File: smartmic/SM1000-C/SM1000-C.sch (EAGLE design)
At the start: 194 parts, among them CN1 HDR100-3, CN10 MJ-3523-SMT, CN11 HDR100-3, CN12 DF11-16DS, CN2 MOLEX-MINI-B-SMT, CN3 RASM722PX, CN4 RJ-45, CN5 MJ-3523-SMT, CN6 SJ-3524, CN7 MJ-3523-SMT, CN8 SJ-3524, CN9 MJ-3523-SMT, J1 JMP-2PIN, J3 JMP-2PIN, J4 JMP-2PIN, P1 TPAD50, P10 TPAD50, P11 TPAD50, P12 TPAD50, P13 TPAD50, P14 TPAD50, P15 TPAD50, P16 TPAD50, P17 TPAD50, P18 TPAD50, P19 TPAD50, P2 TPAD50, P20 TPAD50, P3 TPAD50, P4 TPAD50, P5 TPAD50, P6 TPAD50, P7 TPAD50, P8 TPAD50, P9 TPAD50, SW1 SW-BOURNS-7914S, SW2 SW-BOURNS-7914S, SW3 DPDT, SW4 SW-BOURNS-7914S, SW5 SW-BOURNS-7914J, T1 SM-LP-5001, T2 SM-LP-5001, U1 STM32F405, U2 LD3985M33R, U3 STMPS2141, U4 EMIF02-USB03F2, U5 TPS54329E, U6 LMV341, U7 LMV341, U8 LM386M-1, U9 LMV341

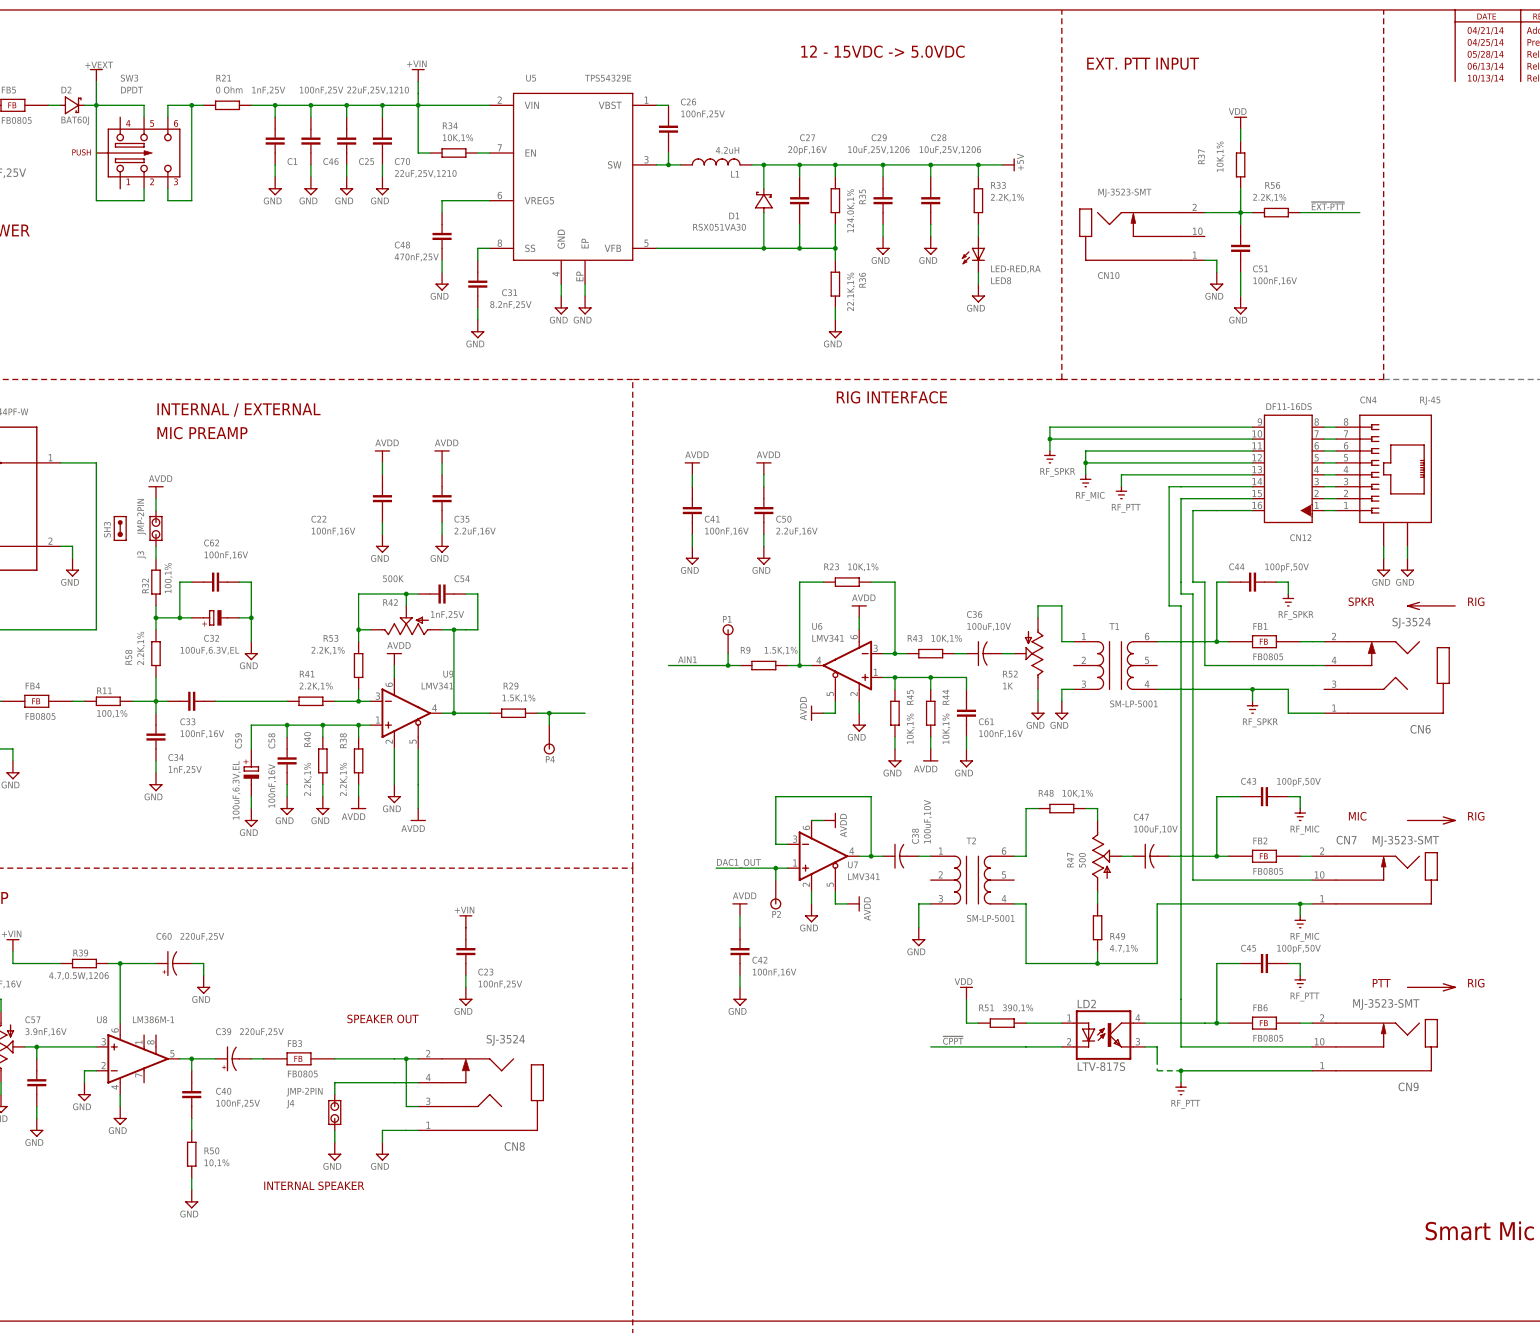
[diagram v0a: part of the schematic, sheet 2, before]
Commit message: Update SM1000-C schematics RGB
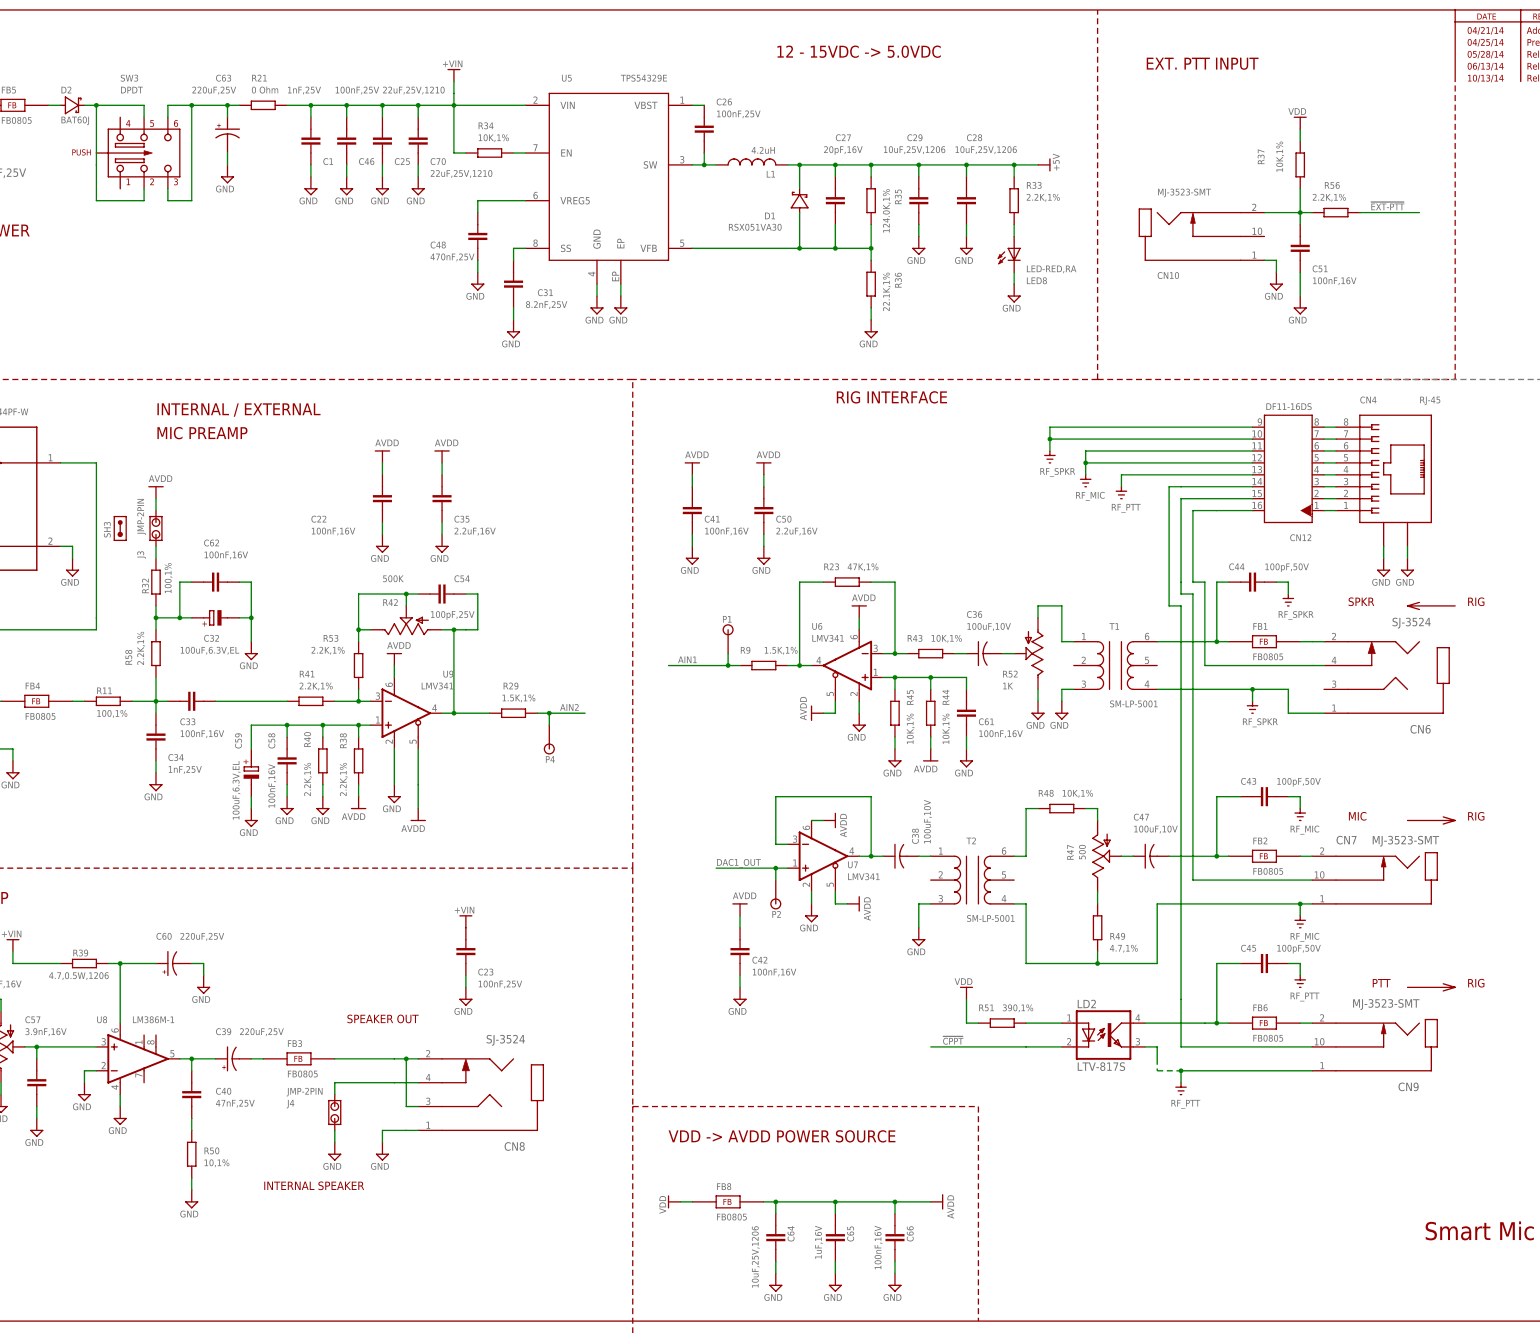
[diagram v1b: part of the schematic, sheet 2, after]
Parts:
- added C63: 220uF,25V, _RoweTel:CAP-CHEMI-MVE-HA0
- added C64: 10uF,25V,1206, ipc-7351-capacitor:CAPACITOR_1206
- added C65: 1uF,16V, AA-ipc-7351-capacitor:CAPACITOR_0603
- added C66: 100nF,16V, AA-ipc-7351-capacitor:CAPACITOR_0603
- added FB8: FB0805, _RoweTel:FB0805
- C40: value 100nF,25V -> 47nF,25V
- C54: value 1nF,25V -> 100pF,25V
- CN3: device _RoweTel:RASM712PX -> _RoweTel:RASM722PX
- R18, R21, R31: device AA-ipc-7351-resistor:RESISTOR_0603 -> AA-ipc-7351-resistor:RESISTOR_0805
- R23: value 10K,1% -> 47K,1%
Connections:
- net +VEXT renamed N$81
- removed net N$36: P4.1, R29.1
- removed net N$81 (its old number): R47.3, R49.2
- new net N$61: R47.1, R49.2
- net AIN2: now also P4.1, R29.1
- net AVDD: now also C64.1, C65.1, C66.1, FB8.2
- net GND: now also C63.2, C64.2, C65.2, C66.2
- net N$70: now also C63.1
- net N$82: now also R47.3; no longer R47.1
- net VDD: now also FB8.1
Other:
- note added: "VDD -> AVDD POWER SOURCE"
- moved on the sheet: C1, C25, C26, C27, C28, C29, C31, C46, C48, C51, C70, CN10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

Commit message: Update Schematic, BOM and add PDFs - RGB
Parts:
- PCB1: value SM1000A -> SM1000C
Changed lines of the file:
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@@
 <part name="B-FRAME2" library="_RoweTel" deviceset="GENERICL-B-SIZE" device=""/>
 <part name="CN2" library="SM1000" deviceset="MOLEX-MINI-B-SMT" device=""/>
-<part name="PCB1" library="_Coherix" deviceset="PCB" device="" value="SM1000A"/>
+<part name="PCB1" library="_Coherix" deviceset="PCB" device="" value="SM1000C"/>
 <part name="V1" library="A-SUPPLY2" deviceset="GND" device=""/>
 <part name="R47" library="_RoweTel" deviceset="TRIMPOT91" device="" value="500"/>
@@
 <text x="421.64" y="264.16" size="1.4224" layer="94" ratio="10">C</text>
 <text x="426.72" y="264.16" size="1.4224" layer="94" ratio="10">RGB</text>
+<wire x1="355.6" y1="264.16" x2="355.6" y2="218.44" width="0.1524" layer="94"/>
+<wire x1="369.57" y1="264.414" x2="369.57" y2="218.44" width="0.1524" layer="94"/>
+<wire x1="414.02" y1="264.16" x2="414.02" y2="218.44" width="0.1524" layer="94"/>
+<wire x1="420.116" y1="263.906" x2="420.37" y2="263.906" width="0.1524" layer="94"/>
+<wire x1="420.37" y1="263.906" x2="420.37" y2="218.44" width="0.1524" layer="94"/>
+<wire x1="425.45" y1="263.906" x2="425.45" y2="218.186" width="0.1524" layer="94"/>
 </plain>
 <instances>
@@
 <segment>
 <pinref part="R26" gate="G$1" pin="1"/>
-<wire x1="203.2" y1="76.2" x2="193.04" y2="76.2" width="0.1524" layer="91"/>
-<label x="193.04" y="76.708" size="1.4224" layer="95" ratio="10"/>
-</segment>
-</net>
+<wire x1="203.2" y1="76.2" x2="190.5" y2="76.2" width="0.1524" layer="91"/>
+<label x="190.5" y="76.708" size="1.4224" layer="95" ratio="10"/>
+</segment>
+</net>

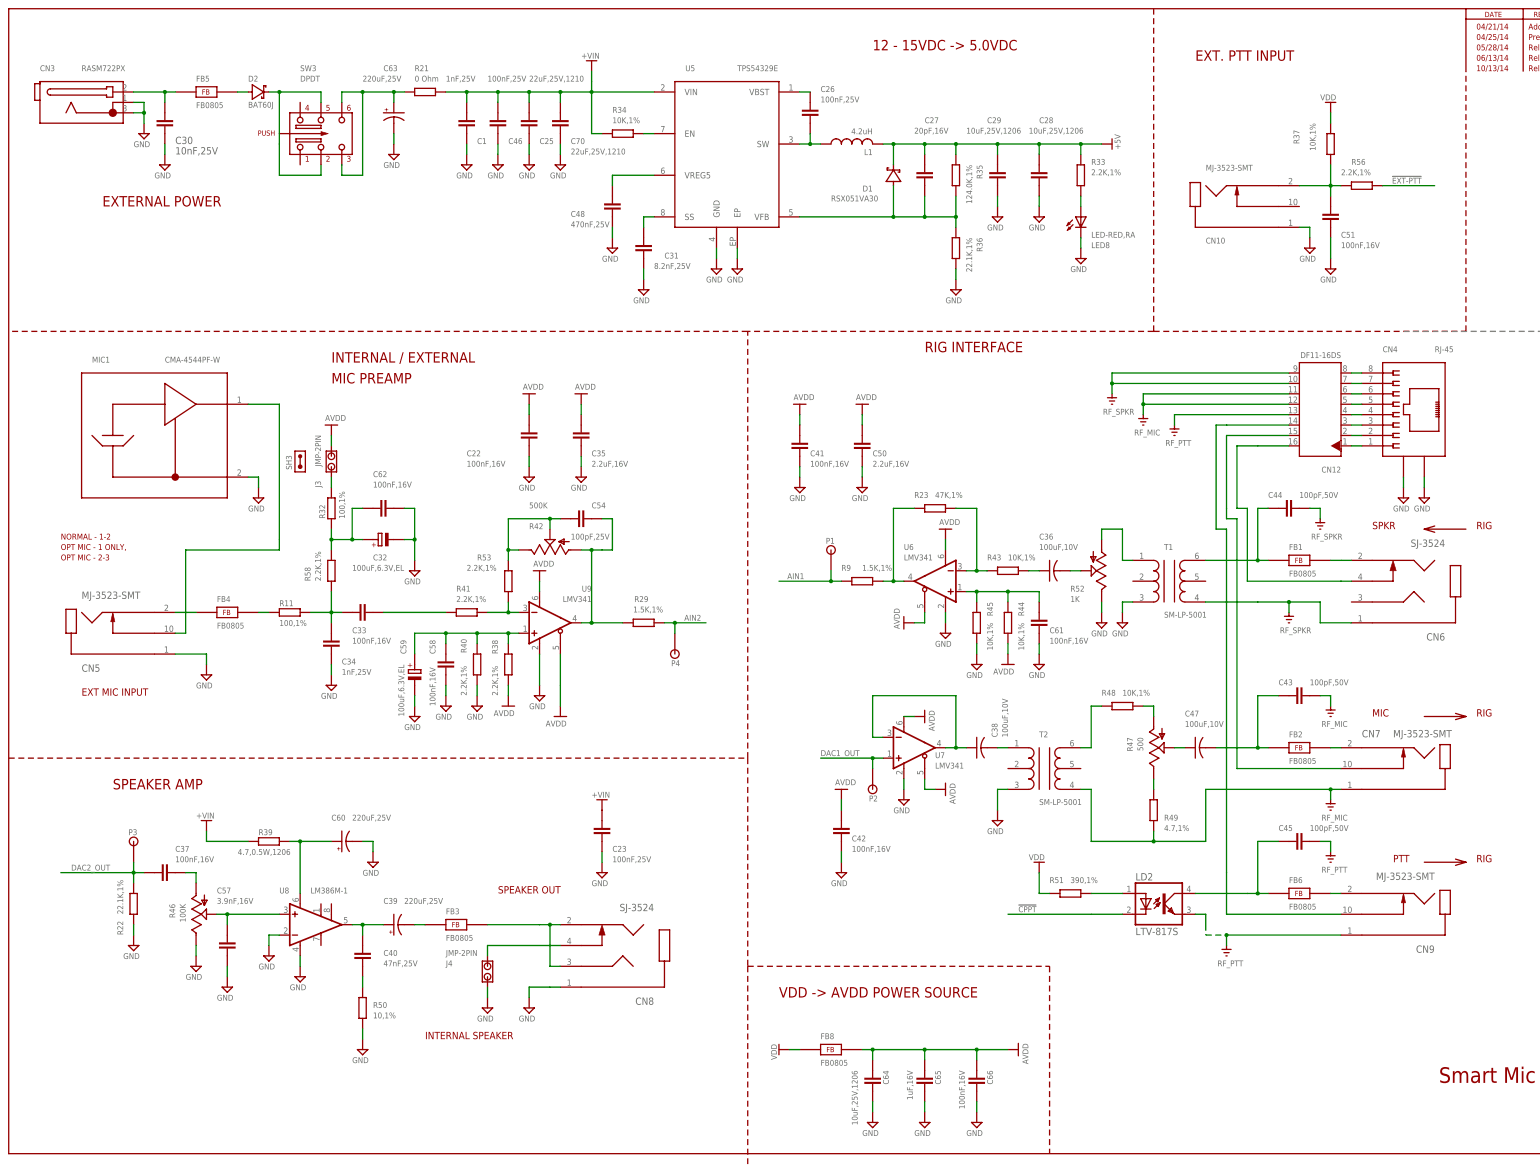
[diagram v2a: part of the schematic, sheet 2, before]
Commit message: Correct Schematic Part Values RGB
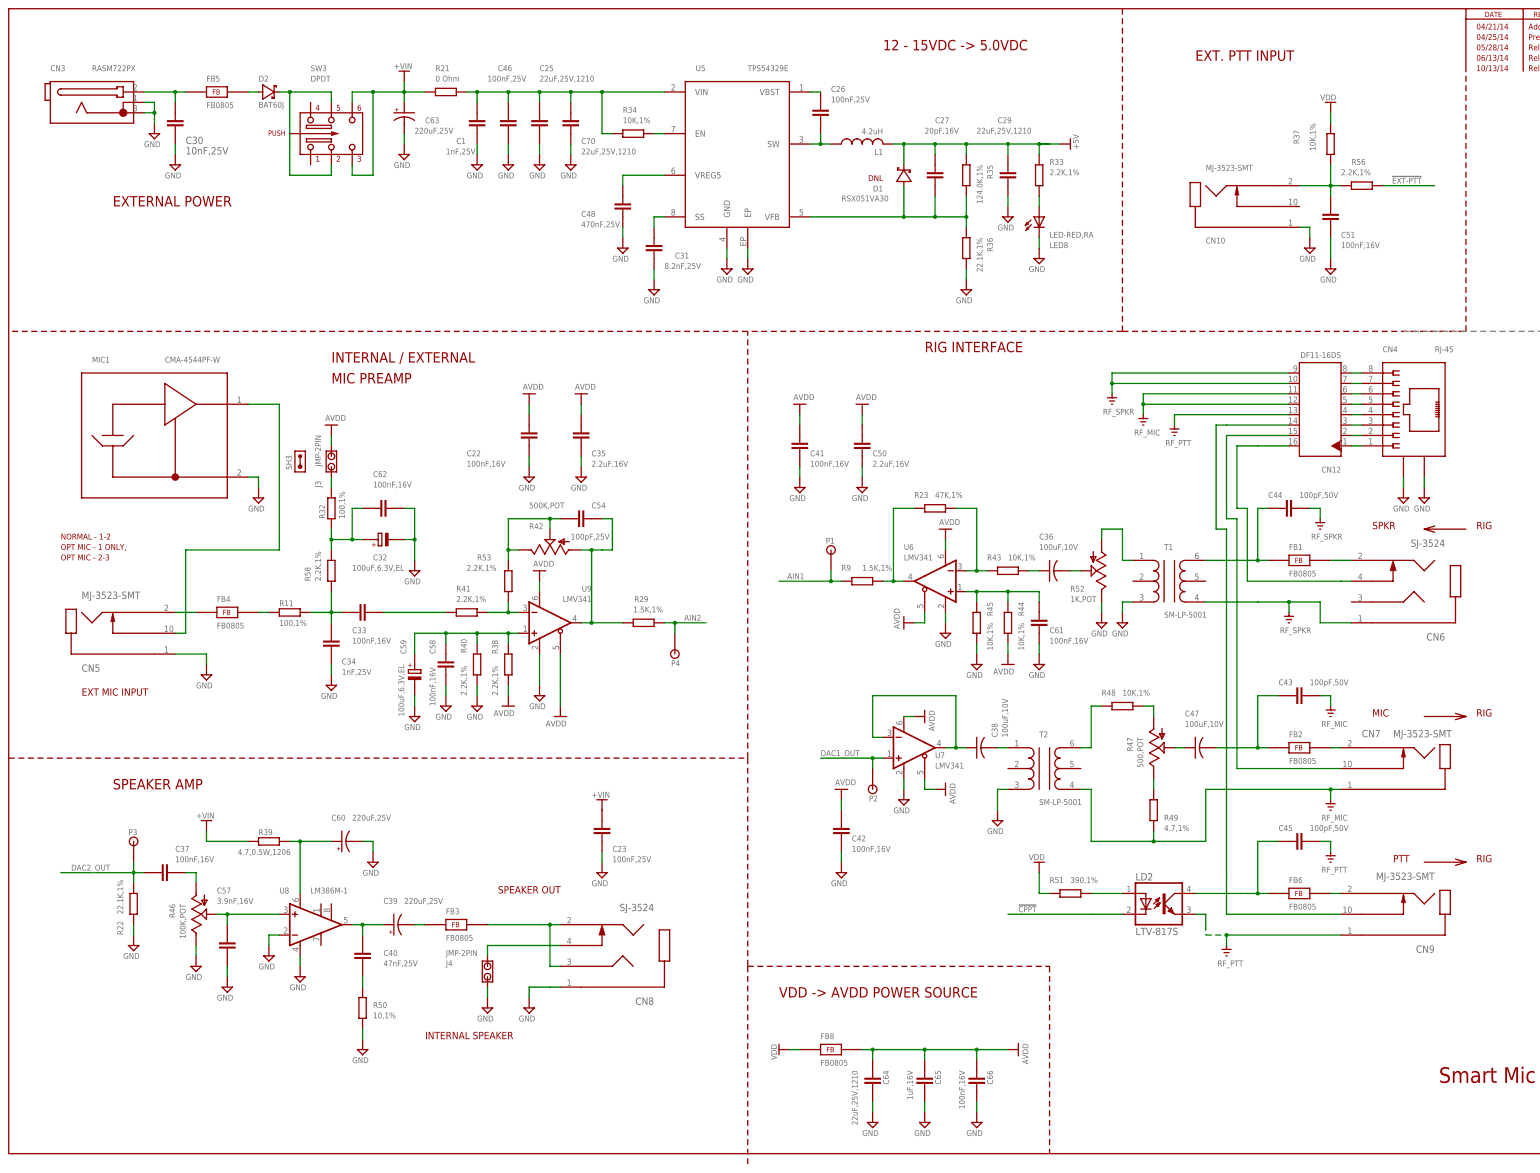
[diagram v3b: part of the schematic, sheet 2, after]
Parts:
- removed C28: 10uF,25V,1206, ipc-7351-capacitor:CAPACITOR_1206
- added SPKR1: SPKR, _RoweTel:SPKR
- C29, C64: value 10uF,25V,1206 -> 22uF,25V,1210; device ipc-7351-capacitor:CAPACITOR_1206 -> AA-ipc-7351-capacitor:CAPACITOR_1210
- C55, C56: value 1nF,16V -> 1nF,25V
- R26, R30, R54, R55: device AA-ipc-7351-resistor:RESISTOR_0603 -> AA-ipc-7351-resistor:RESISTOR_0805
- R42: value 500K -> 500K,POT; device _RoweTel:TRIMPOT91 -> _RoweTel:POT3361
- R46: value 100K -> 100K,POT
- R47: value 500 -> 500,POT; device _RoweTel:TRIMPOT91 -> _RoweTel:POT3361
- R52: value 1K -> 1K,POT; device _RoweTel:TRIMPOT91 -> _RoweTel:POT3361
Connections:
- removed net N$70: C63.1, R21.1, SW3.3, SW3.6
- new net N$36: C1.2, C25.1, C46.1, C70.1, R21.2, R34.1, U5.VIN
- net +5V: no longer C28.1
- net +VIN: now also C63.1, R21.1, SW3.3, SW3.6; no longer C1.2, C25.1, C46.1, C70.1, R21.2, R34.1, U5.VIN
- net GND: no longer C28.2
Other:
- note added: "DNL"
- moved on the sheet: C1, C25, C26, C27, C29, C30, C31, C46, C48, C63, C70, CN3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
